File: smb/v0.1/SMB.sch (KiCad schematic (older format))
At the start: 41 parts, among them IC1 MAX485, IC101 ATMEGA1284-A, IC2 DS2482-100S, J101 RJ45, J102 RTS_RESET, J103 ICSP, J104 SERIAL_REV, P101 I2C_CONN, P102 CONN_10X2, P103 CONN_3X2, P105 CONN_5, P107 CONN_3, P108 CONN_5, P109 CONN_3, P110 CONN_3, P2 CONN_3, SW101 SKQGAKE010, X101 20MHz

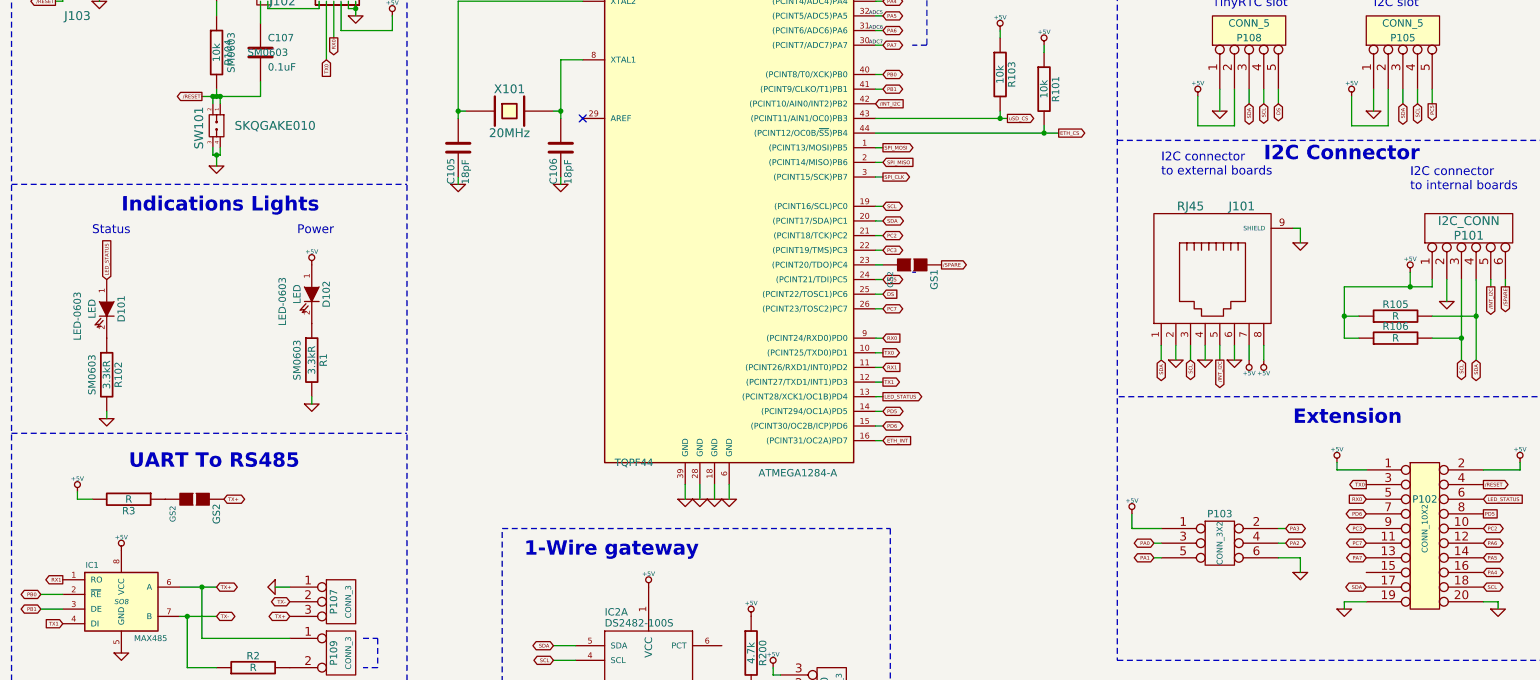
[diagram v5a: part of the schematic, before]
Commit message: suppression pin DS du slot RTC (inutile depuis l'installation d'un DS2408) ajout led 'fault'
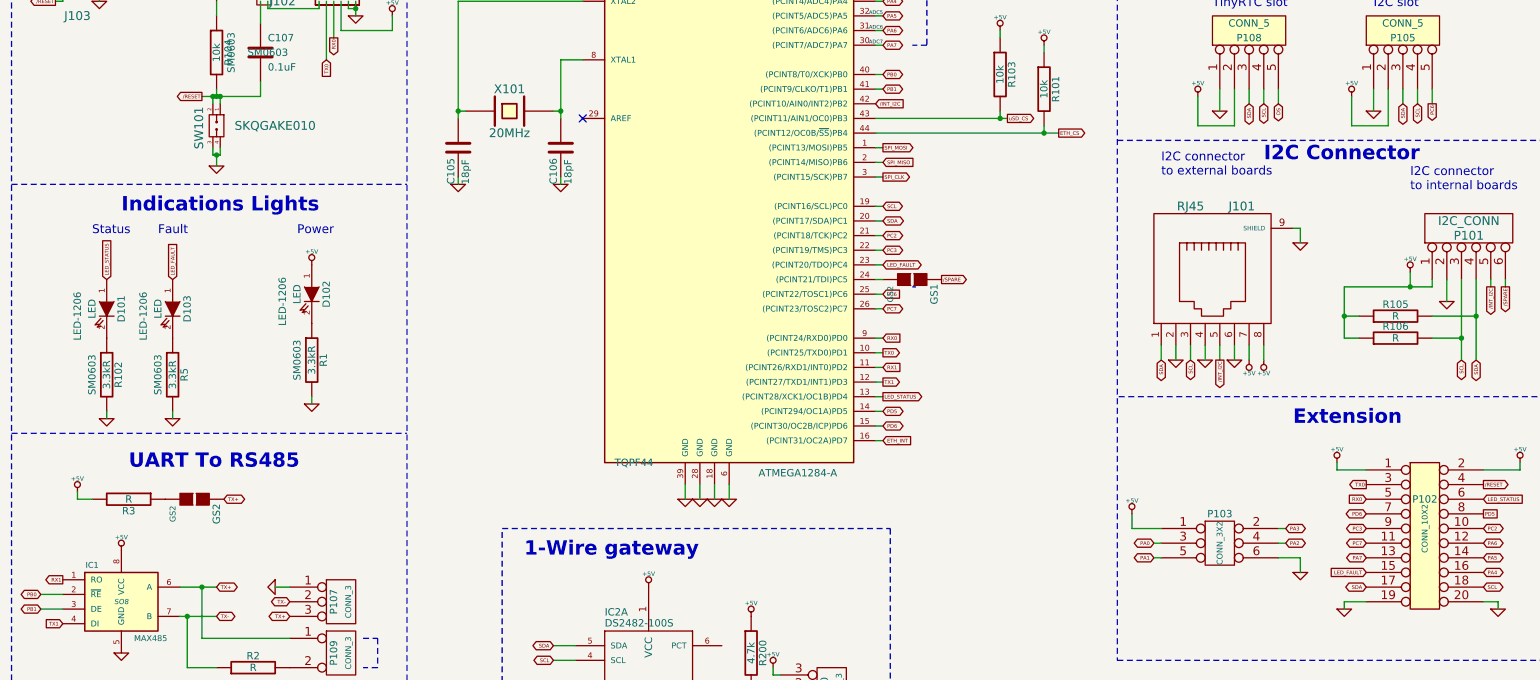
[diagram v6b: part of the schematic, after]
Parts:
- added D103: LED, LED-1206, symbol LED
- added R5: 3.3kR, SM0603, symbol R
- D101, D102: footprint LED-0603 -> LED-1206
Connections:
- net DS: no longer IC101.25 ((PCINT22/TOSC1)PC6)
- net GND: now also R5.2
- net at GS1.2 (G2): now also IC101.24 ((PCINT21/TDI)PC5); no longer IC101.23 ((PCINT20/TDO)PC4)
- net LED_FAULT: now reaches P102.15 (P15)
- net LED_FAULT: now also IC101.23 ((PCINT20/TDO)PC4), D103.1 (A)
- net PC5 renamed PC6
- net PC6: now also IC101.25 ((PCINT22/TOSC1)PC6); no longer IC101.24 ((PCINT21/TDI)PC5)
- new net: D103.2 (K), R5.1
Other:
- note added: "Fault"
- moved on the sheet: GS1
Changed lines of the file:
@@
 F 0 "D101" H 1200 4350 50  0000 C CNN
 F 1 "LED" H 1200 4150 50  0000 C CNN
-F 2 "LED-0603" H 1250 4050 50  0000 C CNN
+F 2 "LED-1206" H 1250 4050 50  0000 C CNN
 F 3 "" H 1200 4250 60  0001 C CNN
 	1    1200 4250
@@
 L GS2 GS1
 U 1 1 503DF9F0
-P 6700 3950
-F 0 "GS1" H 6800 4100 50  0000 C CNN
-F 1 "GS2" H 6800 3801 40  0000 C CNN
-F 2 "" H 6700 3950 60  0001 C CNN
-F 3 "" H 6700 3950 60  0001 C CNN
-	1    6700 3950
+P 6700 4050
+F 0 "GS1" H 6800 4200 50  0000 C CNN
+F 1 "GS2" H 6800 3901 40  0000 C CNN
+F 2 "" H 6700 4050 60  0001 C CNN
+F 3 "" H 6700 4050 60  0001 C CNN
+	1    6700 4050
 	0    1    1    0
 $EndComp
-Text GLabel 6900 3950 2    25   Output ~ 0
+Text GLabel 6900 4050 2    25   Output ~ 0
 /SPARE
 Text GLabel 10750 4100 3    25   Output ~ 0
@@
 F 0 "D102" H 2600 4250 50  0000 C CNN
 F 1 "LED" H 2600 4050 50  0000 C CNN
-F 2 "LED-0603" H 2650 3950 50  0000 C CNN
+F 2 "LED-1206" H 2650 3950 50  0000 C CNN
 F 3 "" H 2600 4150 60  0001 C CNN
 	1    2600 4150
@@
 Text GLabel 6500 3850 2    25   BiDi ~ 0
 PC3
-Text GLabel 6500 4050 2    25   BiDi ~ 0
-PC5
 Text GLabel 6500 4950 2    25   BiDi ~ 0
 PD5
@@
 I2C slot
 Text GLabel 6500 4150 2    25   Input ~ 0
-DS
+PC6
 Text GLabel 10250 2850 3    25   Output ~ 0
-PC5
+PC6
 $Comp
 L CONN_5 P105
@@
 	6450 5050 6500 5050
 Wire Notes Line
-	6700 4000 6725 4000
+	6700 4100 6725 4100
 Wire Wire Line
 	6450 2750 6500 2750
@@
 Text GLabel 10600 6150 2    25   BiDi ~ 0
 SCL
+Text GLabel 6500 3950 2    25   BiDi ~ 0
+LED_FAULT
+$Comp
+L GND #PWR053
+U 1 1 51C6DA80
+P 1650 5000
+F 0 "#PWR053" H 1650 5000 30  0001 C CNN
+F 1 "GND" H 1650 4930 30  0001 C CNN
+F 2 "" H 1650 5000 60  0001 C CNN
+F 3 "" H 1650 5000 60  0001 C CNN
+	1    1650 5000
+	1    0    0    -1
+$EndComp
+$Comp
+L R R5
+U 1 1 51C6DA86
+P 1650 4700
+F 0 "R5" V 1730 4700 50  0000 C CNN
+F 1 "3.3kR" V 1650 4700 50  0000 C CNN
+F 2 "SM0603" V 1550 4700 50  0000 C CNN
+F 3 "" H 1650 4700 60  0001 C CNN
+	1    1650 4700
+	1    0    0    -1
+$EndComp
+$Comp
+L LED D103
+U 1 1 51C6DA8C
+P 1650 4250
+F 0 "D103" H 1650 4350 50  0000 C CNN
+F 1 "LED" H 1650 4150 50  0000 C CNN
+F 2 "LED-1206" H 1700 4050 50  0000 C CNN
+F 3 "" H 1650 4250 60  0001 C CNN
+	1    1650 4250
+	0    1    1    0
+$EndComp
+Text GLabel 1650 4050 1    25   Input ~ 0
+LED_FAULT
+Text Notes 1550 3750 0    60   ~ 0
+Fault
+Wire Wire Line
+	1650 4950 1650 5000
+Text GLabel 9800 6050 0    25   Input ~ 0
+LED_FAULT
 $EndSCHEMATC

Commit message: mis au pas 2.54 ecartement slot i2c inversion connecteur FTDI/leds
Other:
- note removed: "Front Panel Connector"
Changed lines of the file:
@@
 Text GLabel 10600 6050 2    25   BiDi ~ 0
 PA4
-Text Notes 6850 2100 0    60   ~ 0
-Front Panel Connector
 Text Notes 9200 2100 0    98   ~ 20
 I2C SLOT
@@
 Wire Wire Line
 	8350 5950 8400 5950
-Wire Notes Line
-	6700 1750 6800 1750
-Wire Notes Line
-	6800 1750 6800 2450
-Wire Notes Line
-	6800 2450 6700 2450
 Wire Wire Line
 	9200 2850 9200 2750

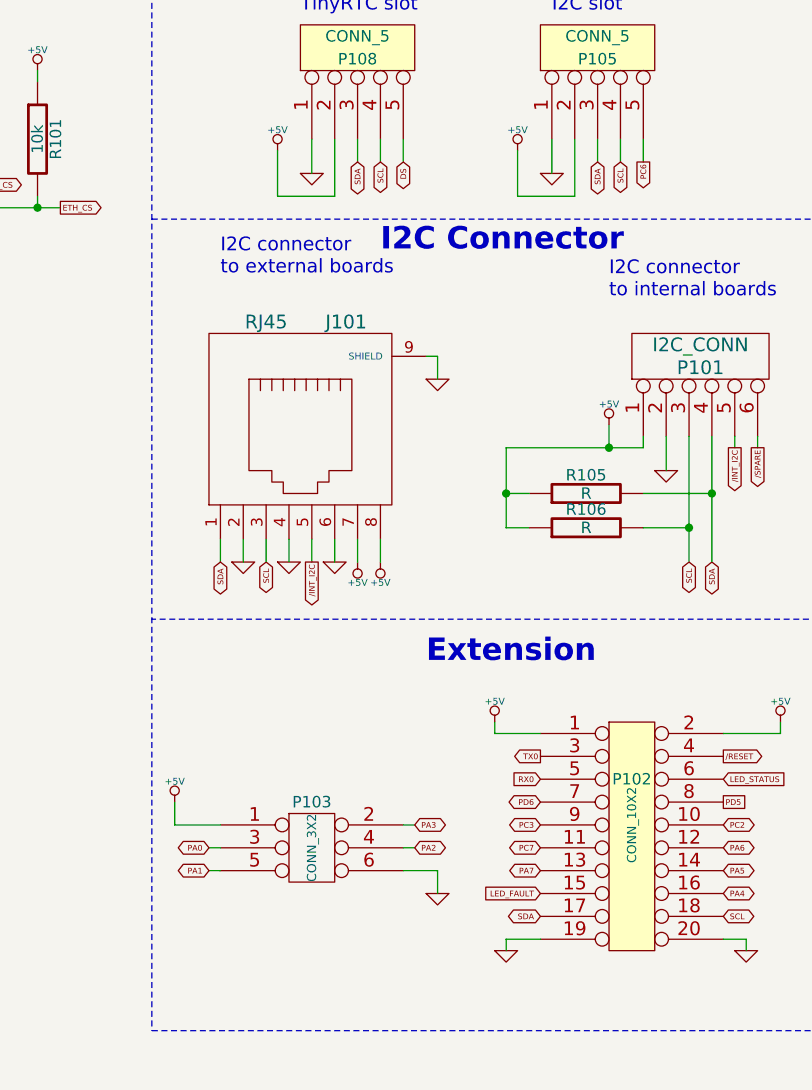
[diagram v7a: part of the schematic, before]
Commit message: creation d'un support type "shield" pour permettre de personnaliser le circuit mis en place d'un mini connecteur 2 points reli?s au shield serigraphie
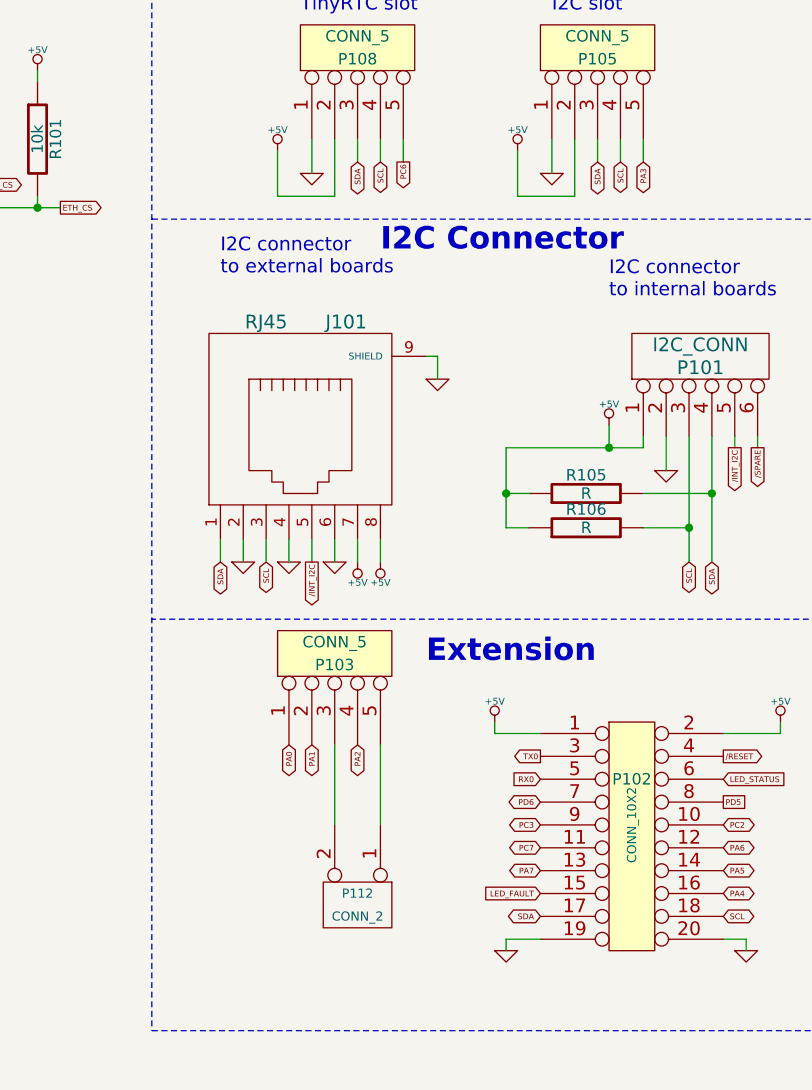
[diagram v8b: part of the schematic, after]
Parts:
- removed P103: CONN_3X2, symbol CONN_3X2
- added P103: CONN_5, ~, symbol CONN_5
- added P112: CONN_2, symbol CONN_2
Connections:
- net DS is gone; now on net PC6: P108.5
- net PA0: now also P103.1
- net PA1: now also P103.2
- net PA2: now also P103.4
- net PA3: now also P105.5
- net PC6: no longer P105.5
- new net: P103.3, P112.2 (PM)
- new net: P103.5, P112.1 (P1)
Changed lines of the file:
@@
 Text GLabel 9800 5650 0    25   BiDi ~ 0
 PD6
-Text GLabel 9200 2850 3    25   BiDi ~ 0
-DS
 Text GLabel 6500 2650 2    25   BiDi ~ 0
 PB0
@@
 Text GLabel 6500 4150 2    25   Input ~ 0
 PC6
-Text GLabel 10250 2850 3    25   Output ~ 0
+Text GLabel 9200 2850 3    25   Output ~ 0
 PC6
 $Comp
@@
 	1    0    0    -1
 $EndComp
-$Comp
-L CONN_3X2 P103
-U 1 1 5195453C
-P 8800 5900
-F 0 "P103" H 8800 6150 50  0000 C CNN
-F 1 "CONN_3X2" V 8800 5950 40  0000 C CNN
-F 2 "" H 8800 5900 60  0001 C CNN
-F 3 "" H 8800 5900 60  0001 C CNN
-	1    8800 5900
-	1    0    0    -1
-$EndComp
-$Comp
-L GND #PWR038
-U 1 1 51954713
-P 9350 6050
-F 0 "#PWR038" H 9350 6050 30  0001 C CNN
-F 1 "GND" H 9350 5980 30  0001 C CNN
-F 2 "" H 9350 6050 60  0001 C CNN
-F 3 "" H 9350 6050 60  0001 C CNN
-	1    9350 6050
-	1    0    0    -1
-$EndComp
-Text GLabel 9250 5750 2    25   BiDi ~ 0
+Text GLabel 10250 2850 3    25   BiDi ~ 0
 PA3
-Text GLabel 8350 5950 0    25   BiDi ~ 0
+Text GLabel 8800 5400 3    25   BiDi ~ 0
 PA1
-Text GLabel 9250 5850 2    25   BiDi ~ 0
+Text GLabel 9000 5400 3    25   BiDi ~ 0
 PA2
-Text GLabel 8350 5850 0    25   BiDi ~ 0
+Text GLabel 8700 5400 3    25   BiDi ~ 0
 PA0
 Text GLabel 10600 5950 2    25   BiDi ~ 0
@@
 Power
 $Comp
-L GND #PWR039
+L GND #PWR038
 U 1 1 5198A43C
 P 9350 3800
-F 0 "#PWR039" H 9350 3800 30  0001 C CNN
+F 0 "#PWR038" H 9350 3800 30  0001 C CNN
 F 1 "GND" H 9350 3730 30  0001 C CNN
 F 2 "" H 9350 3800 60  0001 C CNN
@@
 $EndComp
 $Comp
-L GND #PWR040
+L GND #PWR039
 U 1 1 519D1DAE
 P 950 6950
-F 0 "#PWR040" H 950 6950 30  0001 C CNN
+F 0 "#PWR039" H 950 6950 30  0001 C CNN
 F 1 "GND" H 950 6880 30  0001 C CNN
 F 2 "" H 950 6950 60  0001 C CNN
@@
 $EndComp
 $Comp
-L +5V #PWR041
+L +5V #PWR040
 U 1 1 519D1DB4
 P 1000 5500
-F 0 "#PWR041" H 1000 5590 20  0001 C CNN
+F 0 "#PWR040" H 1000 5590 20  0001 C CNN
 F 1 "+5V" H 1000 5590 30  0000 C CNN
 F 2 "" H 1000 5500 60  0001 C CNN
@@
 $EndComp
 $Comp
-L GND #PWR042
+L GND #PWR041
 U 1 1 519D1FD2
 P 2350 6150
-F 0 "#PWR042" H 2350 6150 30  0001 C CNN
+F 0 "#PWR041" H 2350 6150 30  0001 C CNN
 F 1 "GND" H 2350 6080 30  0001 C CNN
 F 2 "" H 2350 6150 60  0001 C CNN
@@
 $EndComp
 $Comp
-L GND #PWR043
+L GND #PWR042
 U 1 1 51B21010
 P 4150 7100
-F 0 "#PWR043" H 4150 7100 30  0001 C CNN
+F 0 "#PWR042" H 4150 7100 30  0001 C CNN
 F 1 "GND" H 4150 7030 30  0001 C CNN
 F 2 "" H 4150 7100 60  0000 C CNN
@@
 $EndComp
 $Comp
-L GND #PWR044
+L GND #PWR043
 U 1 1 51B21128
 P 5750 7050
-F 0 "#PWR044" H 5750 7050 30  0001 C CNN
+F 0 "#PWR043" H 5750 7050 30  0001 C CNN
 F 1 "GND" H 5750 6980 30  0001 C CNN
 F 2 "" H 5750 7050 60  0000 C CNN
@@
 $EndComp
 $Comp
-L +5V #PWR045
+L +5V #PWR044
 U 1 1 51B212F9
 P 5750 6700
-F 0 "#PWR045" H 5750 6790 20  0001 C CNN
+F 0 "#PWR044" H 5750 6790 20  0001 C CNN
 F 1 "+5V" H 5750 6790 30  0000 C CNN
 F 2 "" H 5750 6700 60  0000 C CNN
@@
 $EndComp
 $Comp
-L GND #PWR046
+L GND #PWR045
 U 1 1 51B21A6C
 P 4900 7350
-F 0 "#PWR046" H 4900 7350 30  0001 C CNN
+F 0 "#PWR045" H 4900 7350 30  0001 C CNN
 F 1 "GND" H 4900 7280 30  0001 C CNN
 F 2 "" H 4900 7350 60  0000 C CNN
@@
 $EndComp
 $Comp
-L +5V #PWR047
+L +5V #PWR046
 U 1 1 51B21C07
 P 4900 6150
-F 0 "#PWR047" H 4900 6240 20  0001 C CNN
+F 0 "#PWR046" H 4900 6240 20  0001 C CNN
 F 1 "+5V" H 4900 6240 30  0000 C CNN
 F 2 "" H 4900 6150 60  0000 C CNN
@@
 $EndComp
 $Comp
-L +5V #PWR048
+L +5V #PWR047
 U 1 1 51B21C1D
 P 5600 6350
-F 0 "#PWR048" H 5600 6440 20  0001 C CNN
+F 0 "#PWR047" H 5600 6440 20  0001 C CNN
 F 1 "+5V" H 5600 6440 30  0000 C CNN
 F 2 "" H 5600 6350 60  0000 C CNN
@@
 PC7
 $Comp
-L +5V #PWR049
+L +5V #PWR048
 U 1 1 51BDB124
 P 10850 5300
-F 0 "#PWR049" H 10850 5390 20  0001 C CNN
+F 0 "#PWR048" H 10850 5390 20  0001 C CNN
 F 1 "+5V" H 10850 5390 30  0000 C CNN
 F 2 "" H 10850 5300 60  0001 C CNN
@@
 $EndComp
 $Comp
-L GND #PWR050
+L GND #PWR049
 U 1 1 51BDB20B
 P 9650 6300
-F 0 "#PWR050" H 9650 6300 30  0001 C CNN
+F 0 "#PWR049" H 9650 6300 30  0001 C CNN
 F 1 "GND" H 9650 6230 30  0001 C CNN
 F 2 "" H 9650 6300 60  0001 C CNN
@@
 	10700 6250 10700 6300
 Wire Wire Line
-	8200 5750 8400 5750
-Wire Wire Line
-	8200 5650 8200 5750
-Wire Wire Line
-	9200 5950 9350 5950
-Wire Wire Line
-	9350 5950 9350 6050
-Wire Wire Line
-	9200 5750 9250 5750
-Wire Wire Line
-	9200 5850 9250 5850
-Wire Wire Line
-	8350 5850 8400 5850
-Wire Wire Line
-	8350 5950 8400 5950
-Wire Wire Line
 	9200 2850 9200 2750
 Wire Notes Line
@@
 Wire Notes Line
 	11100 6650 11100 5850
-$Comp
-L +5V #PWR051
-U 1 1 51BE1AAF
-P 8200 5650
-F 0 "#PWR051" H 8200 5740 20  0001 C CNN
-F 1 "+5V" H 8200 5740 30  0000 C CNN
-F 2 "" H 8200 5650 60  0001 C CNN
-F 3 "" H 8200 5650 60  0001 C CNN
-	1    8200 5650
-	1    0    0    -1
-$EndComp
 $Comp
 L CONN_3 P2
@@
 Connection ~ 5750 6950
 $Comp
-L +5V #PWR052
+L +5V #PWR050
 U 1 1 51C581D7
 P 5400 7100
-F 0 "#PWR052" H 5400 7190 20  0001 C CNN
+F 0 "#PWR050" H 5400 7190 20  0001 C CNN
 F 1 "+5V" H 5400 7190 30  0000 C CNN
 F 2 "" H 5400 7100 60  0000 C CNN
@@
 LED_FAULT
 $Comp
-L GND #PWR053
+L GND #PWR051
 U 1 1 51C6DA80
 P 1650 5000
-F 0 "#PWR053" H 1650 5000 30  0001 C CNN
+F 0 "#PWR051" H 1650 5000 30  0001 C CNN
 F 1 "GND" H 1650 4930 30  0001 C CNN
 F 2 "" H 1650 5000 60  0001 C CNN
@@
 Text GLabel 9800 6050 0    25   Input ~ 0
 LED_FAULT
+$Comp
+L CONN_5 P103
+U 1 1 51C9E212
+P 8900 5000
+F 0 "P103" V 8850 5000 50  0000 C CNN
+F 1 "CONN_5" V 8950 5000 50  0000 C CNN
+F 2 "~" H 8900 5000 60  0000 C CNN
+F 3 "~" H 8900 5000 60  0000 C CNN
+	1    8900 5000
+	0    -1   -1   0
+$EndComp
+$Comp
+L CONN_2 P112
+U 1 1 51C9F32F
+P 9000 6100
+F 0 "P112" V 8950 6100 40  0000 C CNN
+F 1 "CONN_2" V 9050 6100 40  0000 C CNN
+F 2 "" H 9000 6100 60  0000 C CNN
+F 3 "" H 9000 6100 60  0000 C CNN
+	1    9000 6100
+	0    1    1    0
+$EndComp
+Wire Wire Line
+	8900 5400 8900 5750
+Wire Wire Line
+	9100 5400 9100 5750
 $EndSCHEMATC
